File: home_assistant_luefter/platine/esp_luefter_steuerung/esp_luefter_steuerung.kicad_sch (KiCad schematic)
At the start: 7 parts, among them J1 Conn_01x04_Pin, J2 Conn_01x04_Pin, J3 Conn_01x04_Pin, J4 PWR Input 12V, U1 WeMos_D1_mini, U2 LM7805_TO220

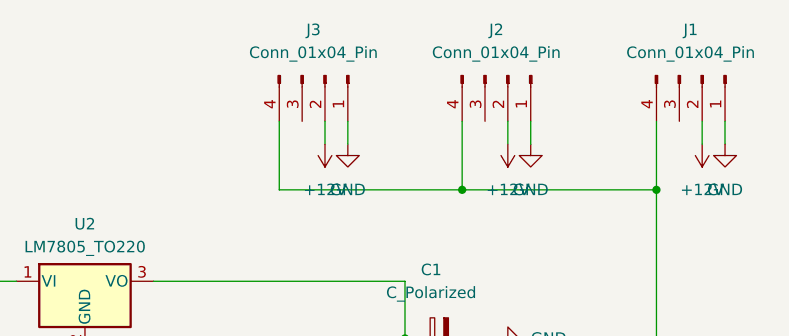
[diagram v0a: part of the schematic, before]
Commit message: increase trace widths
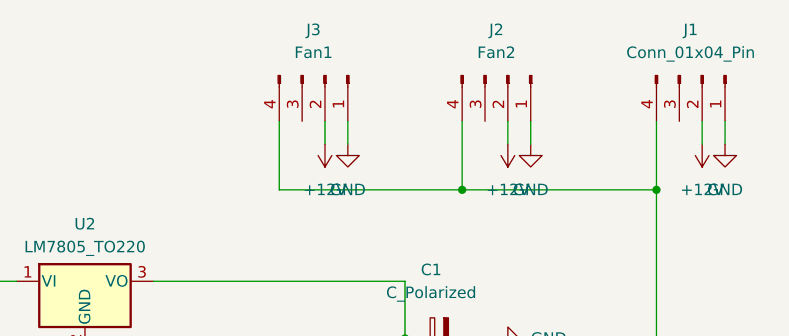
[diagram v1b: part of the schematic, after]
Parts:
- J2: value Conn_01x04_Pin -> Fan2
- J3: value Conn_01x04_Pin -> Fan1
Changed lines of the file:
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@@
 			)
 		)
-		(property "Value" "Conn_01x04_Pin"
+		(property "Value" "Fan2"
 			(at 138.43 39.37 90)
 			(effects
@@
 			)
 		)
-		(property "Value" "Conn_01x04_Pin"
+		(property "Value" "Fan1"
 			(at 118.11 39.37 90)
 			(effects
